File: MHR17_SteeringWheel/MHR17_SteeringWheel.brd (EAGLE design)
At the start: 38.1 x 38.1 mm, 2 parts, among them IC1 AT90CAN128

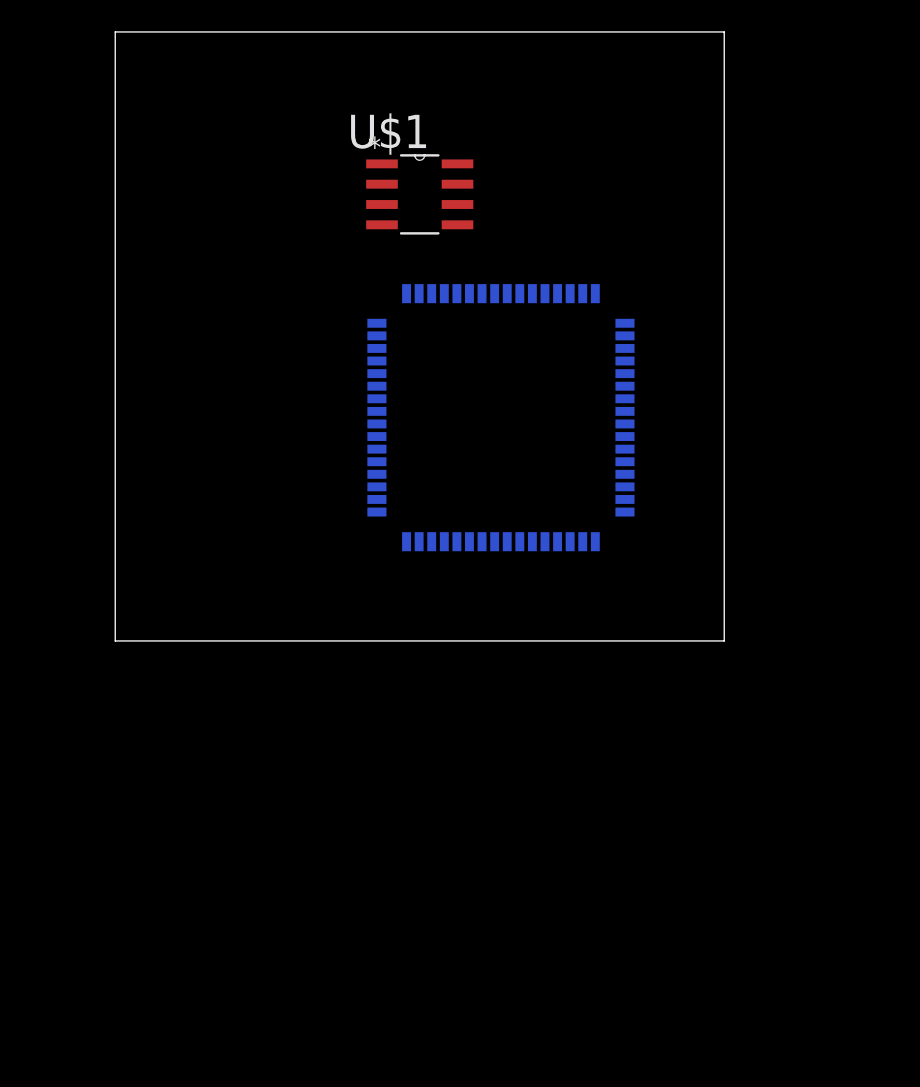
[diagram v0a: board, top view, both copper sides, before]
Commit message: added output ports, still need to check wiresize
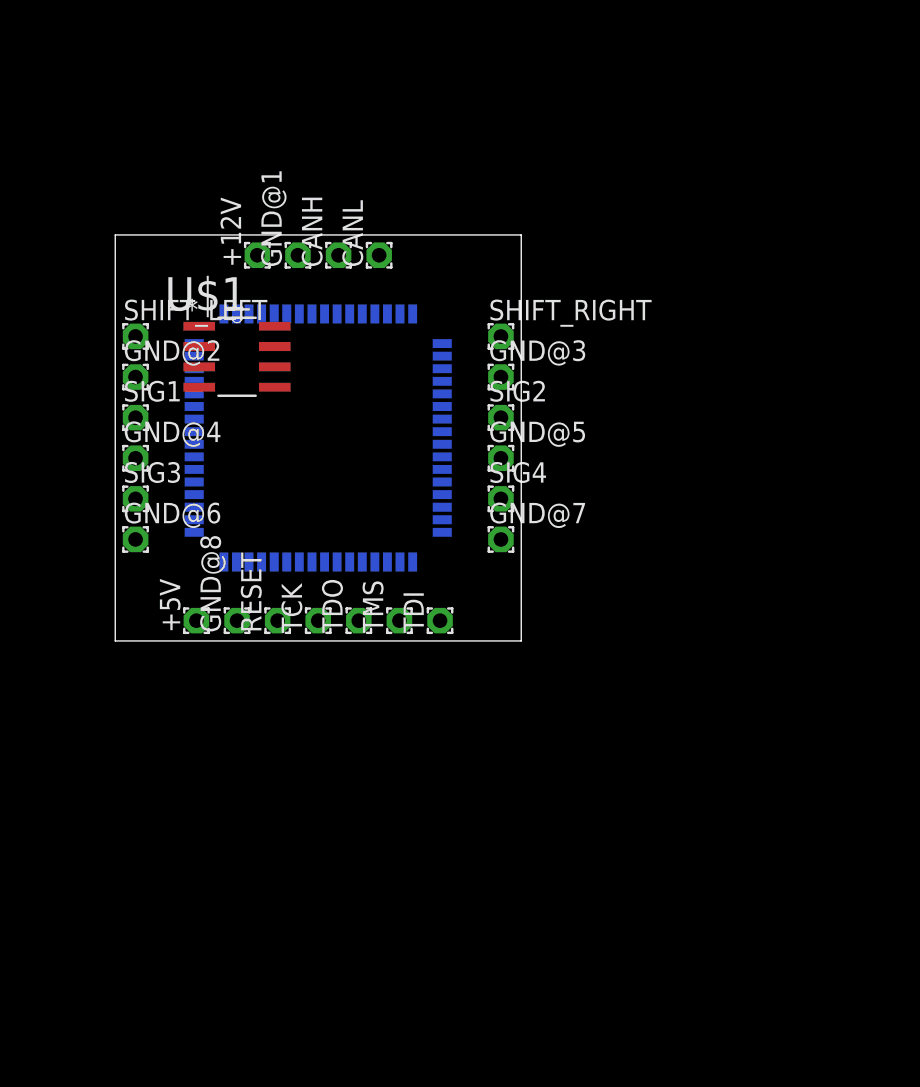
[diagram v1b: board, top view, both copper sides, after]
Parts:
- added +12V, +5V, CANH, CANL, GND@1, GND@2, GND@3, GND@4, GND@5, GND@6, GND@7, GND@8, RESET, SHIFT_LEFT, SHIFT_RIGHT, SIG1, SIG2, SIG3, SIG4, TCK, TDI, TDO, TMS: WIREPAD1,6/0,9, wirepad:1,6/0,9
- moved U$1 15.3 mm to (7.62, 17.8)
- moved IC1 11.5 mm to (12.7, 12.7)
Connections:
- removed net VCC: IC1.21
- new net +5V: +5V.1, IC1.21, IC1.52
- new net 12V: +12V.1
- new net CANH: CANH.1
- new net CANL: CANL.1
- new net N$12: IC1.19
- new net N$13: IC1.18
- new net N$14: IC1.43
- new net N$15: IC1.34
- new net N$16: IC1.33
- new net N$21: IC1.58
- new net N$22: IC1.59
- new net N$23: IC1.60
- new net N$24: IC1.61
- new net N$25: IC1.44
- new net N$26: IC1.45
- new net N$27: IC1.46
- new net N$28: IC1.47
- new net N$29: IC1.48
- new net N$3: IC1.23
- new net N$30: IC1.49
- new net N$31: IC1.50
- new net N$32: IC1.51
- new net N$33: IC1.17
- new net N$34: IC1.16
- new net N$35: IC1.15
- new net N$36: IC1.14
- new net N$37: IC1.13
- new net N$38: IC1.12
- new net N$39: IC1.11
- new net N$4: IC1.24
- new net N$40: IC1.10
- new net N$41: IC1.42
- new net N$42: IC1.41
- new net N$43: IC1.40
- new net N$44: IC1.39
- new net N$45: IC1.38
- new net N$46: IC1.37
- new net N$47: IC1.36
- new net N$48: IC1.35
- new net N$49: IC1.32
- new net N$5: IC1.62
- new net N$50: IC1.31
- new net N$51: IC1.30
- new net N$52: IC1.29
- new net N$53: IC1.28
- new net N$54: IC1.27
- new net N$55: IC1.26
- new net N$56: IC1.25
- new net N$57: IC1.9
- new net N$58: IC1.8
- new net N$59: IC1.7
- new net N$6: IC1.64
- new net N$60: IC1.6
- new net N$61: IC1.5
- new net N$62: IC1.4
- new net N$63: IC1.3
- new net N$64: IC1.2
- new net RESET: IC1.20, RESET.1
- new net SHIFT_LEFT: SHIFT_LEFT.1
- new net SHIFT_RIGHT: SHIFT_RIGHT.1
- new net SIG1: SIG1.1
- new net SIG2: SIG2.1
- new net SIG3: SIG3.1
- new net SIG4: SIG4.1
- new net TCK: IC1.57, TCK.1
- new net TDI: IC1.54, TDI.1
- new net TDO: IC1.55, TDO.1
- new net TMS: IC1.56, TMS.1
- net GND: now also GND@1.1, GND@2.1, GND@3.1, GND@4.1, GND@5.1, GND@6.1, GND@7.1, GND@8.1, IC1.53, IC1.63
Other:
- board size 38.1 x 38.1 mm -> 25.4 x 25.4 mm

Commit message: added frame for schematic
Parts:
- moved U$1 10.8 mm to (18.4, 17.8), turned to 90 degrees
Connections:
- net VDD renamed N$9
- new net N$1: U$1.4
- new net N$10: U$1.1
- new net N$11: U$1.8
- new net N$17: U$1.2
- new net N$2: U$1.5
- net CANH: now also U$1.7
- net CANL: now also U$1.6
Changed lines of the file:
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@@
 <elements>
 <element name="IC1" library="at90can128" package="TQFP64" value="AT90CAN128" x="12.7" y="12.7" rot="MR0"/>
-<element name="U$1" library="Microchip_By_element14_Batch_1" package="SOIC127P600X175-8N" value="MCP2551-I/SN" x="7.62" y="17.78">
-<attribute name="PACKAGE" value="SOIC-8" x="7.62" y="17.78" size="1.778" layer="27" display="off"/>
-<attribute name="SUPPLIER" value="Microchip" x="7.62" y="17.78" size="1.778" layer="27" display="off"/>
-<attribute name="MPN" value="MCP2551-I/SN" x="7.62" y="17.78" size="1.778" layer="27" display="off"/>
-<attribute name="OC_FARNELL" value="9758569" x="7.62" y="17.78" size="1.778" layer="27" display="off"/>
-<attribute name="OC_NEWARK" value="69K7604" x="7.62" y="17.78" size="1.778" layer="27" display="off"/>
+<element name="U$1" library="Microchip_By_element14_Batch_1" package="SOIC127P600X175-8N" value="MCP2551-I/SN" x="18.415" y="17.78" rot="R90">
+<attribute name="PACKAGE" value="SOIC-8" x="18.415" y="17.78" size="1.778" layer="27" rot="R90" display="off"/>
+<attribute name="SUPPLIER" value="Microchip" x="18.415" y="17.78" size="1.778" layer="27" rot="R90" display="off"/>
+<attribute name="MPN" value="MCP2551-I/SN" x="18.415" y="17.78" size="1.778" layer="27" rot="R90" display="off"/>
+<attribute name="OC_FARNELL" value="9758569" x="18.415" y="17.78" size="1.778" layer="27" rot="R90" display="off"/>
+<attribute name="OC_NEWARK" value="69K7604" x="18.415" y="17.78" size="1.778" layer="27" rot="R90" display="off"/>
 </element>
 <element name="+12V" library="wirepad" package="1,6/0,9" value="WIREPAD1,6/0,9" x="8.89" y="24.13" rot="R90"/>
@@
 <wire x1="1.27" y1="16.51" x2="7.62" y2="1.27" width="0" layer="19" extent="1-1"/>
 </signal>
-<signal name="VDD">
-<contactref element="U$1" pad="3"/>
-</signal>
 <signal name="CANH">
 <contactref element="CANH" pad="1"/>
+<contactref element="U$1" pad="7"/>
+<wire x1="17.78" y1="20.1422" x2="13.97" y2="24.13" width="0" layer="19" extent="1-1"/>
 </signal>
 <signal name="CANL">
 <contactref element="CANL" pad="1"/>
+<contactref element="U$1" pad="6"/>
+<wire x1="19.05" y1="20.1422" x2="16.51" y2="24.13" width="0" layer="19" extent="1-1"/>
 </signal>
 <signal name="SHIFT_LEFT">
@@
 <contactref element="IC1" pad="2"/>
 </signal>
+<signal name="N$1">
+<contactref element="U$1" pad="4"/>
+</signal>
+<signal name="N$2">
+<contactref element="U$1" pad="5"/>
+</signal>
+<signal name="N$9">
+<contactref element="U$1" pad="3"/>
+</signal>
+<signal name="N$10">
+<contactref element="U$1" pad="1"/>
+</signal>
+<signal name="N$11">
+<contactref element="U$1" pad="8"/>
+</signal>
+<signal name="N$17">
+<contactref element="U$1" pad="2"/>
+</signal>
 </signals>

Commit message: changed dimensions and added power for various ports
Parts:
- added C1, C2: 20nF, rcl:C0603
- added C3, C4, C5: 100nF, rcl:C0603
- added Q1: (no value), crystal:HC49/S
- moved GND@3 12.1 mm to (36.2, 16.5)
- moved GND@5 12.1 mm to (36.2, 11.4)
- moved GND@7 12.1 mm to (36.2, 6.35)
- moved SHIFT_RIGHT 12.1 mm to (36.2, 19.1)
- moved SIG2 12.1 mm to (36.2, 14.0)
- moved SIG4 12.1 mm to (36.2, 8.89)
- moved U$1 3.81 mm to (14.6, 17.8)
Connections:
- removed net N$5: IC1.62
- removed net N$6: IC1.64
- net +5V: now also C3.1, C4.1, C5.1, IC1.62, IC1.64
- net GND: now also C1.1, C2.1, C3.2, C4.2, C5.2
- net N$3: now also C1.2, Q1.2
- net N$4: now also C2.2, Q1.1
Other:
- board size 25.4 x 25.4 mm -> 38.1 x 25.4 mm
